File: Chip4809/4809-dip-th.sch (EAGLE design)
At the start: 20 parts, among them Q1 32768

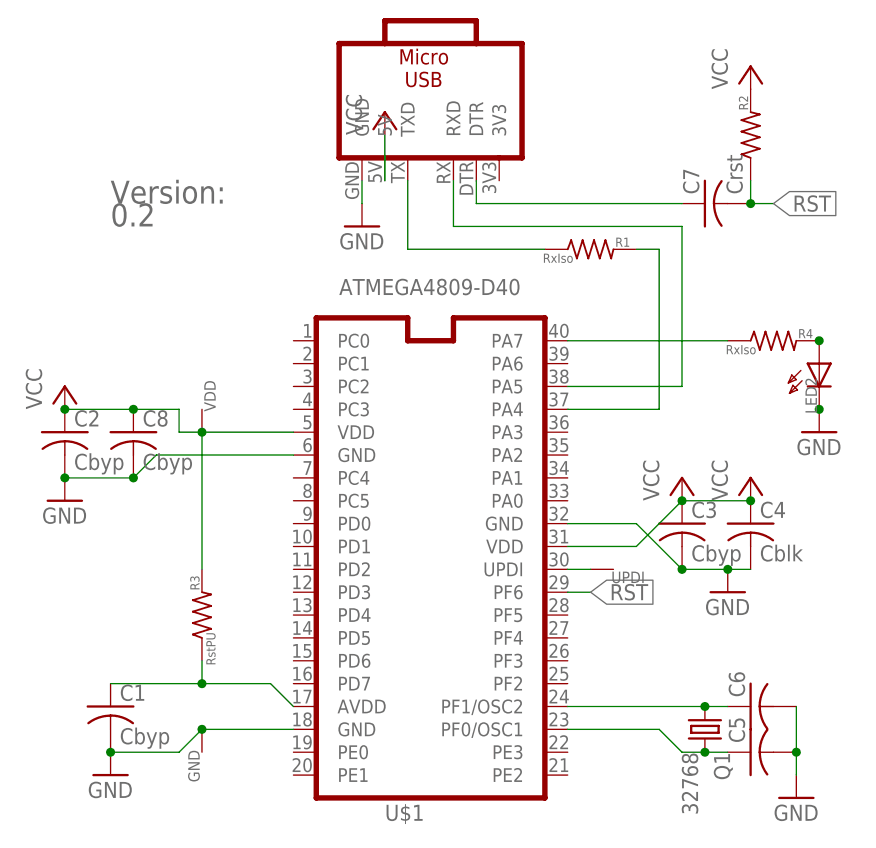
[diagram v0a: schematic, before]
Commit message: Version 0.4 fix RX/TX, move UPDI pin
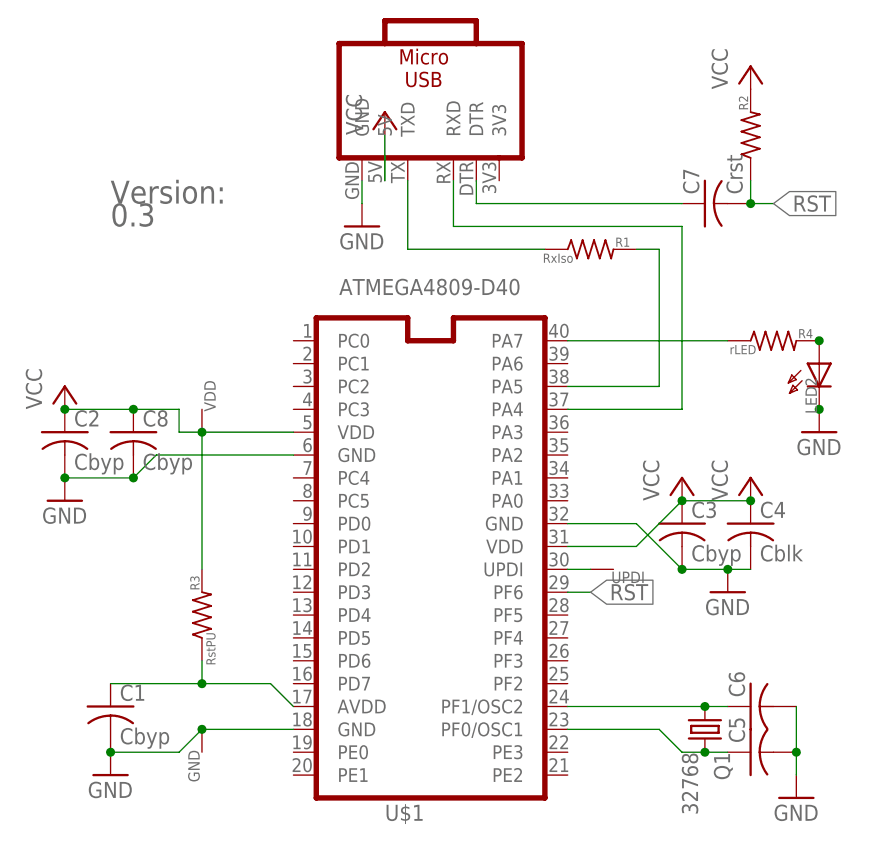
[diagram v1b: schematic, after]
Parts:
- R4: value RxIso -> rLED
- VS1: value 0.2 -> 0.3
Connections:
- removed net CPURX: R1.2, U$1.PA4
- removed net CPUTX: MOD1.RXD, U$1.PA5
- new net N$3: R1.2, U$1.PA5
- new net N$4: MOD1.RXD, U$1.PA4
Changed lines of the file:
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@@
 <part name="R3" library="my-rcl" deviceset="R-US_" device="R0805" value="RstPU"/>
 <part name="C8" library="my-rcl" deviceset="C-US" device="C1206" value="Cbyp"/>
-<part name="VS1" library="mylib4" deviceset="VERSIONSTRING" device="" value="0.2"/>
-<part name="R4" library="my-rcl" deviceset="R-US_" device="0204/7" value="RxIso"/>
+<part name="VS1" library="mylib4" deviceset="VERSIONSTRING" device="" value="0.3"/>
+<part name="R4" library="my-rcl" deviceset="R-US_" device="0204/7" value="rLED"/>
 <part name="GND5" library="supply1" deviceset="GND" device=""/>
 <part name="LED2" library="mylib4" deviceset="LED" device="3MM"/>
@@
 </segment>
 </net>
-<net name="CPUTX" class="0">
-<segment>
-<pinref part="U$1" gate="G$1" pin="PA5"/>
-<wire x1="76.2" y1="63.5" x2="88.9" y2="63.5" width="0.1524" layer="91"/>
-<wire x1="88.9" y1="63.5" x2="88.9" y2="81.28" width="0.1524" layer="91"/>
-<pinref part="MOD1" gate="G$1" pin="RXD"/>
-<wire x1="63.5" y1="86.36" x2="63.5" y2="81.28" width="0.1524" layer="91"/>
-<wire x1="88.9" y1="81.28" x2="63.5" y2="81.28" width="0.1524" layer="91"/>
-</segment>
-</net>
-<net name="CPURX" class="0">
-<segment>
-<pinref part="U$1" gate="G$1" pin="PA4"/>
-<wire x1="76.2" y1="60.96" x2="86.36" y2="60.96" width="0.1524" layer="91"/>
-<wire x1="86.36" y1="60.96" x2="86.36" y2="78.74" width="0.1524" layer="91"/>
-<pinref part="R1" gate="G$1" pin="2"/>
-<wire x1="86.36" y1="78.74" x2="83.82" y2="78.74" width="0.1524" layer="91"/>
-</segment>
-</net>
 <net name="USBTX" class="0">
 <segment>
@@
 </segment>
 </net>
+<net name="N$3" class="0">
+<segment>
+<pinref part="R1" gate="G$1" pin="2"/>
+<wire x1="83.82" y1="78.74" x2="86.36" y2="78.74" width="0.1524" layer="91"/>
+<wire x1="86.36" y1="78.74" x2="86.36" y2="63.5" width="0.1524" layer="91"/>
+<pinref part="U$1" gate="G$1" pin="PA5"/>
+<wire x1="86.36" y1="63.5" x2="76.2" y2="63.5" width="0.1524" layer="91"/>
+</segment>
+</net>
+<net name="N$4" class="0">
+<segment>
+<pinref part="MOD1" gate="G$1" pin="RXD"/>
+<wire x1="63.5" y1="86.36" x2="63.5" y2="81.28" width="0.1524" layer="91"/>
+<wire x1="63.5" y1="81.28" x2="88.9" y2="81.28" width="0.1524" layer="91"/>
+<wire x1="88.9" y1="81.28" x2="88.9" y2="60.96" width="0.1524" layer="91"/>
+<pinref part="U$1" gate="G$1" pin="PA4"/>
+<wire x1="88.9" y1="60.96" x2="76.2" y2="60.96" width="0.1524" layer="91"/>
+</segment>
+</net>
